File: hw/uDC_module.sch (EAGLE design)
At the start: 38 parts, among them J1 GROVE-4P-2.0-3470130P1, J2 GROVE-4P-2.0-3470130P1, U5 LD3985XX, X1 22-23-2021, X2 22-23-2021, X3 53047-06, X4 53047-06

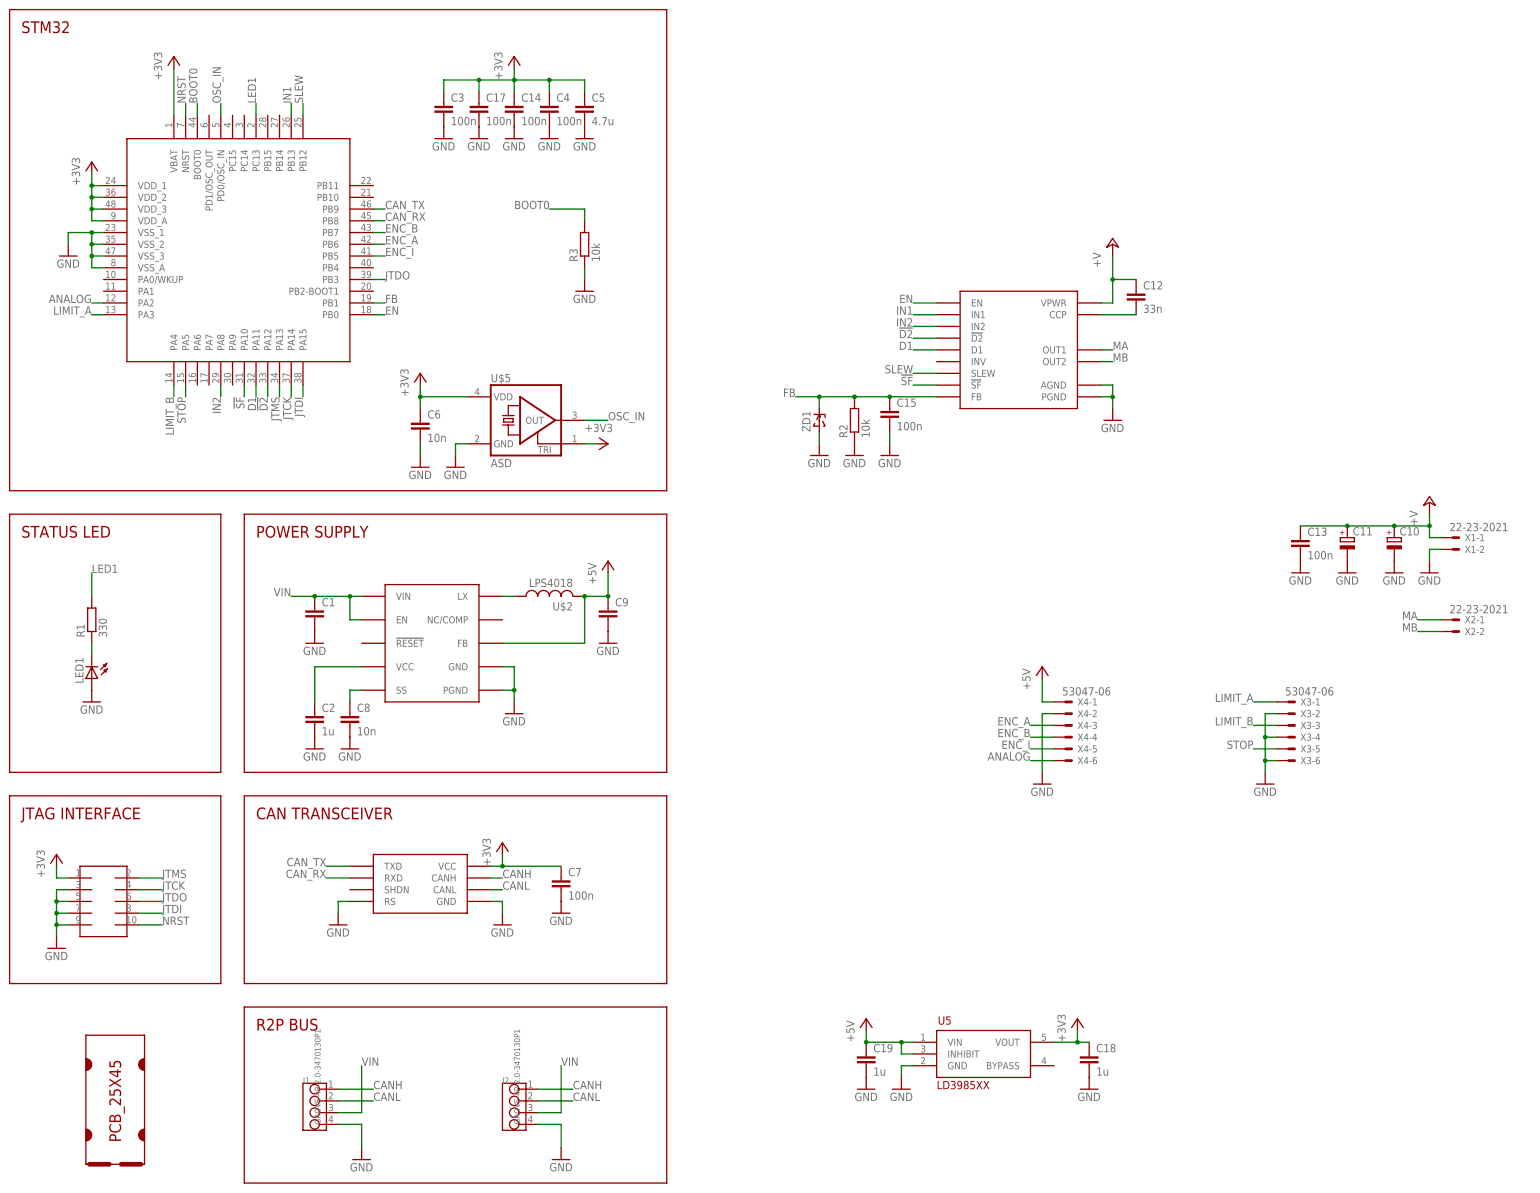
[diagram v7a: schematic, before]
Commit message: moved IN2 to TIM1 ch2
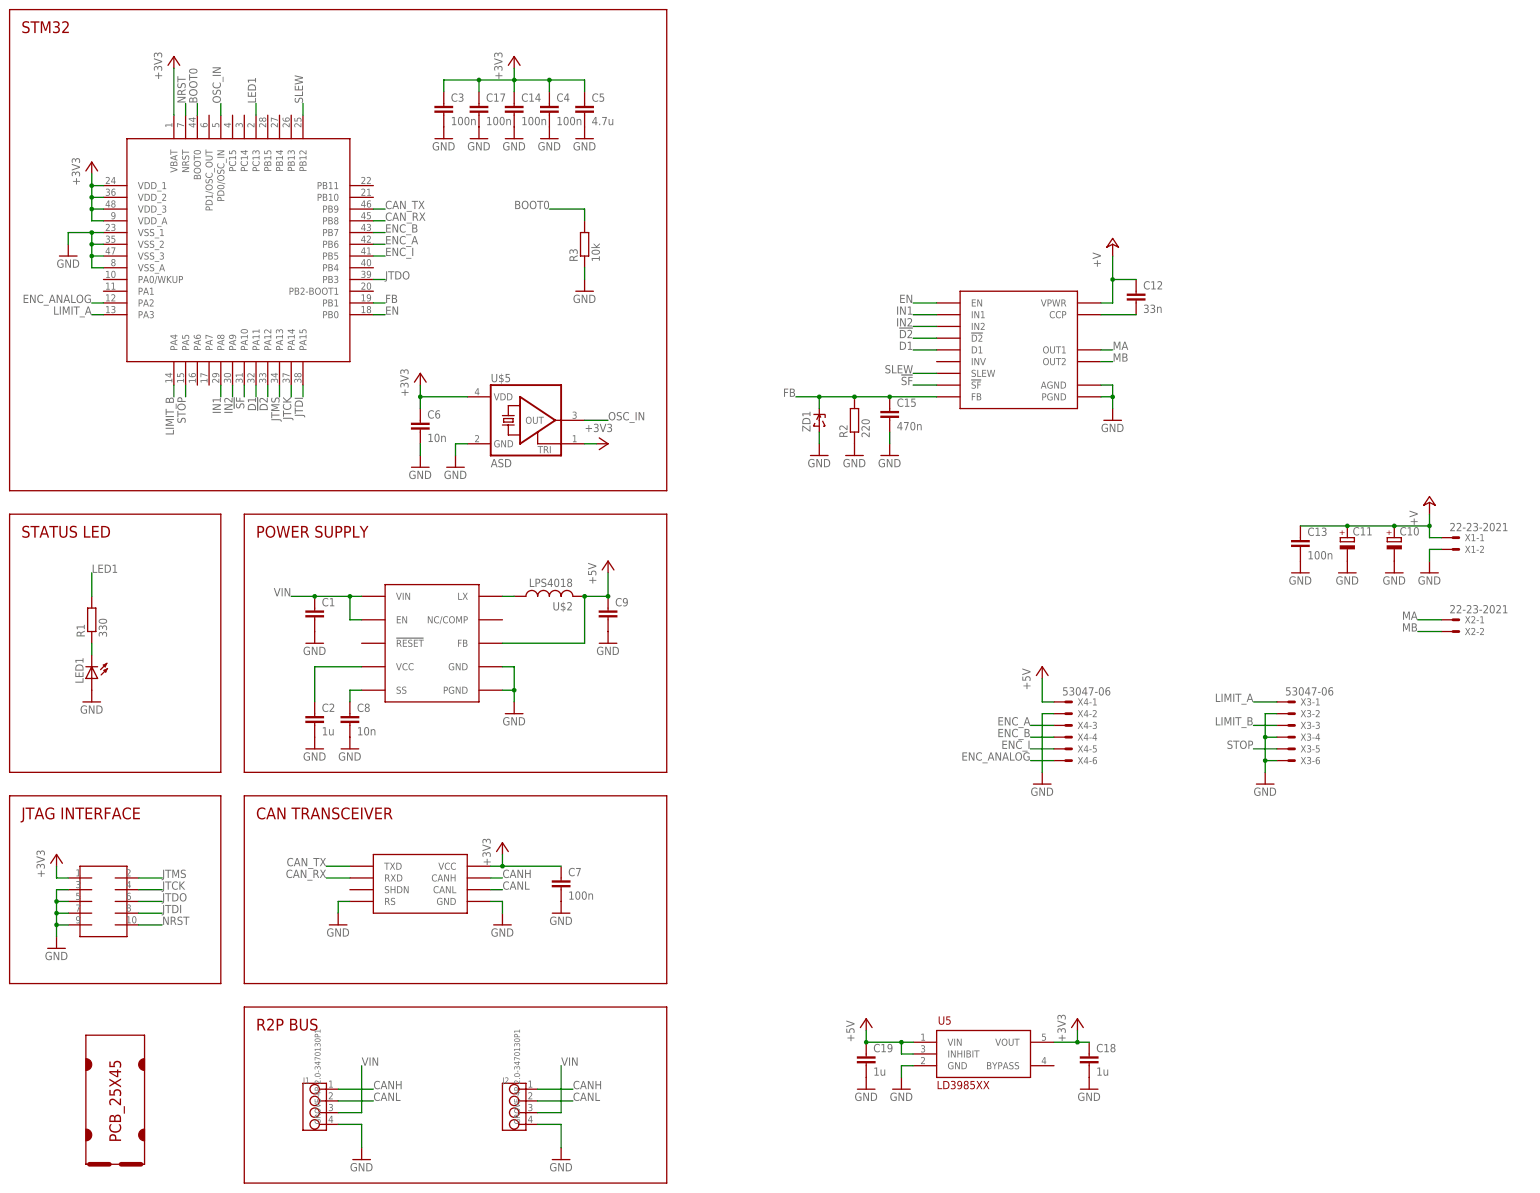
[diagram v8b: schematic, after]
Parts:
- C15: value 100n -> 470n
- R2: value 10k -> 220
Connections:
- net ANALOG renamed ENC_ANALOG
- net IN1: now also U$6.PA8; no longer U$6.PB13
- net IN2: now also U$6.PA9; no longer U$6.PA8
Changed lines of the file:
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@@
 <?xml version="1.0" encoding="utf-8"?>
 <!DOCTYPE eagle SYSTEM "eagle.dtd">
-<eagle version="6.4">
+<eagle version="6.6.0">
 <drawing>
 <settings>
@@
 <part name="C13" library="rcl" deviceset="C-EU" device="C0603" value="100n"/>
 <part name="GND21" library="supply1" deviceset="GND" device=""/>
-<part name="C15" library="rcl" deviceset="C-EU" device="C0603" value="100n"/>
-<part name="R2" library="rcl" deviceset="R-EU_" device="R0603" value="10k"/>
+<part name="C15" library="rcl" deviceset="C-EU" device="C0603" value="470n"/>
+<part name="R2" library="rcl" deviceset="R-EU_" device="R0603" value="220"/>
 <part name="GND23" library="supply" deviceset="GND" device=""/>
 <part name="GND24" library="supply" deviceset="GND" device=""/>
@@
 </segment>
 <segment>
+<pinref part="U$6" gate="G$1" pin="PA9"/>
+<wire x1="53.34" y1="177.8" x2="53.34" y2="175.26" width="0.1524" layer="91"/>
+<label x="53.34" y="175.26" size="1.778" layer="95" rot="MR270"/>
+</segment>
+</net>
+<net name="IN1" class="0">
+<segment>
+<wire x1="205.74" y1="193.04" x2="200.66" y2="193.04" width="0.1524" layer="91"/>
+<label x="200.66" y="193.04" size="1.778" layer="95" rot="MR0"/>
+<pinref part="U$7" gate="G$1" pin="IN1"/>
+</segment>
+<segment>
 <pinref part="U$6" gate="G$1" pin="PA8"/>
 <wire x1="50.8" y1="177.8" x2="50.8" y2="175.26" width="0.1524" layer="91"/>
 <label x="50.8" y="175.26" size="1.778" layer="95" rot="MR270"/>
-</segment>
-</net>
-<net name="IN1" class="0">
-<segment>
-<wire x1="205.74" y1="193.04" x2="200.66" y2="193.04" width="0.1524" layer="91"/>
-<label x="200.66" y="193.04" size="1.778" layer="95" rot="MR0"/>
-<pinref part="U$7" gate="G$1" pin="IN1"/>
-</segment>
-<segment>
-<pinref part="U$6" gate="G$1" pin="PB13"/>
-<wire x1="66.04" y1="236.22" x2="66.04" y2="238.76" width="0.1524" layer="91"/>
-<label x="66.04" y="238.76" size="1.778" layer="95" rot="R90"/>
 </segment>
 </net>
@@
 </segment>
 </net>
-<net name="ANALOG" class="0">
+<net name="ENC_ANALOG" class="0">
 <segment>
 <pinref part="X4" gate="-6" pin="S"/>
